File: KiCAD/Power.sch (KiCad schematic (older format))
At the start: 13 parts, among them J301 UJC-HP-3-SMT-TR, SW302 KXT 331 LHS

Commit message: Continue work on Schematics
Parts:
- removed BC301: BQ25157, XasPrints:DSBGA-20, symbol XasParts:BQ25157
- removed FID301: Fiducial, XasPrints:LiPo_150mAh, symbol Mechanical:Fiducial
- removed R301: 5k 0402, Resistor_SMD:R_0402_1005Metric, symbol Device:R_Small
- removed SW302: KXT 331 LHS, Button_Switch_SMD:SW_SPST_CK_KXT3, symbol Switch:SW_Push
- added CH301: BQ24232, Package_DFN_QFN:VQFN-16-1EP_3x3mm_P0.5mm_EP1.6x1.6mm_ThermalVias, symbol XasParts:BQ24232
- added R301, R302: 10k 0402, Resistor_SMD:R_0402_1005Metric, symbol Device:R
- added R? (x2): R_Small, symbol Device:R_Small
- added SW301: MIC94069, XasPrints:MLF-6-EP-P0.5mm, symbol XasParts:MIC94069
- C303: value 2.2uF 0402 -> 1uF 0603 16V; footprint Capacitor_SMD:C_0402_1005Metric -> Capacitor_SMD:C_0603_1608Metric
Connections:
- net labels added: +5V, MAIN_PWR_ON
- net labels removed: SCL, SDA
- wire segments 67 -> 83
- no-connect marks 5 -> 6
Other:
- moved on the sheet: BT301, C301, C302, C304, C305, D301, J301, PW301

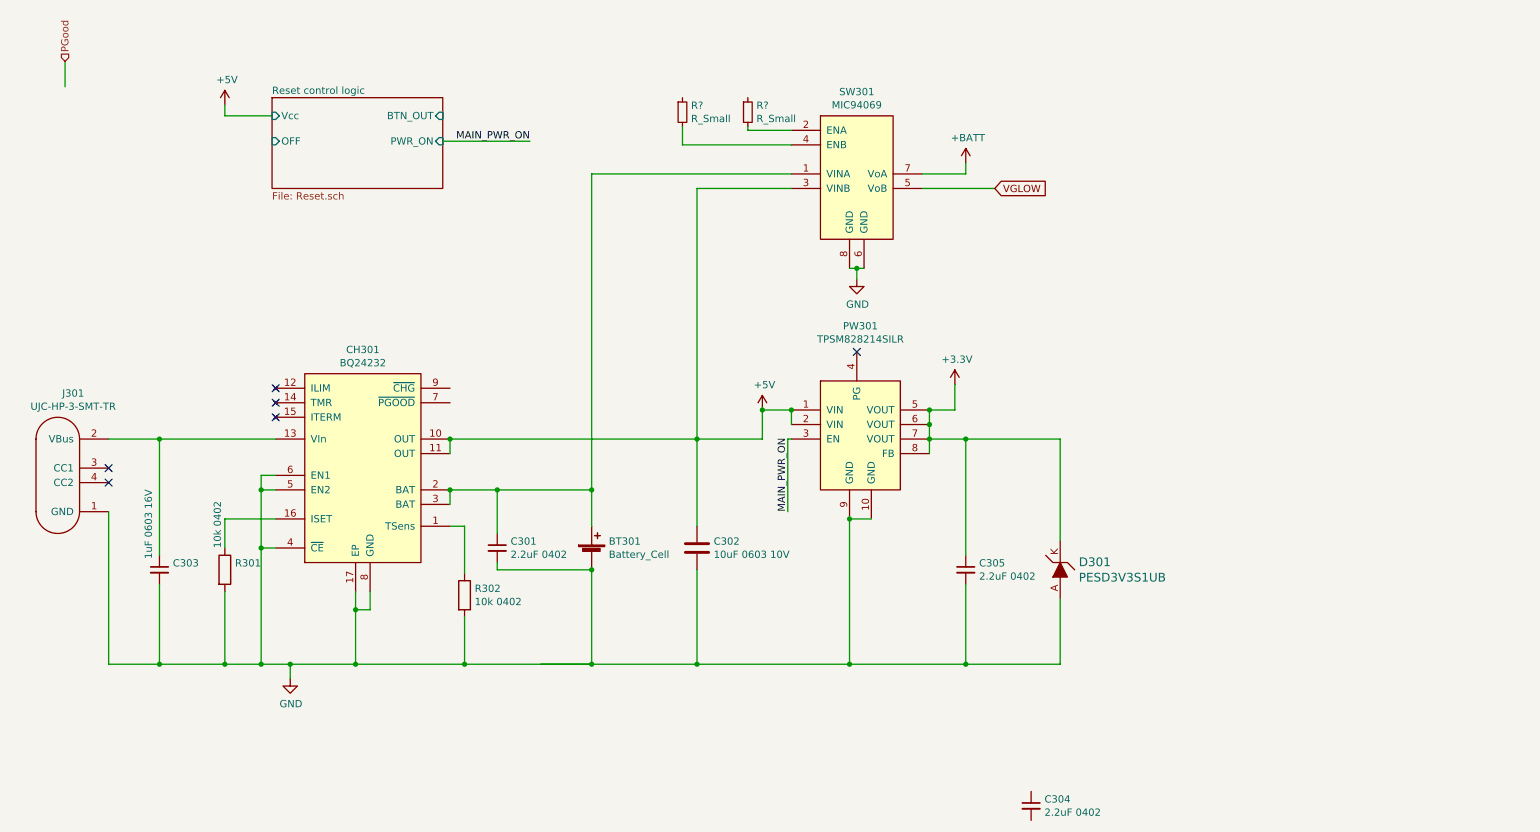
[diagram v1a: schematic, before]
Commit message: Add STM32 base circuit for power control and USB, also a lot of other things
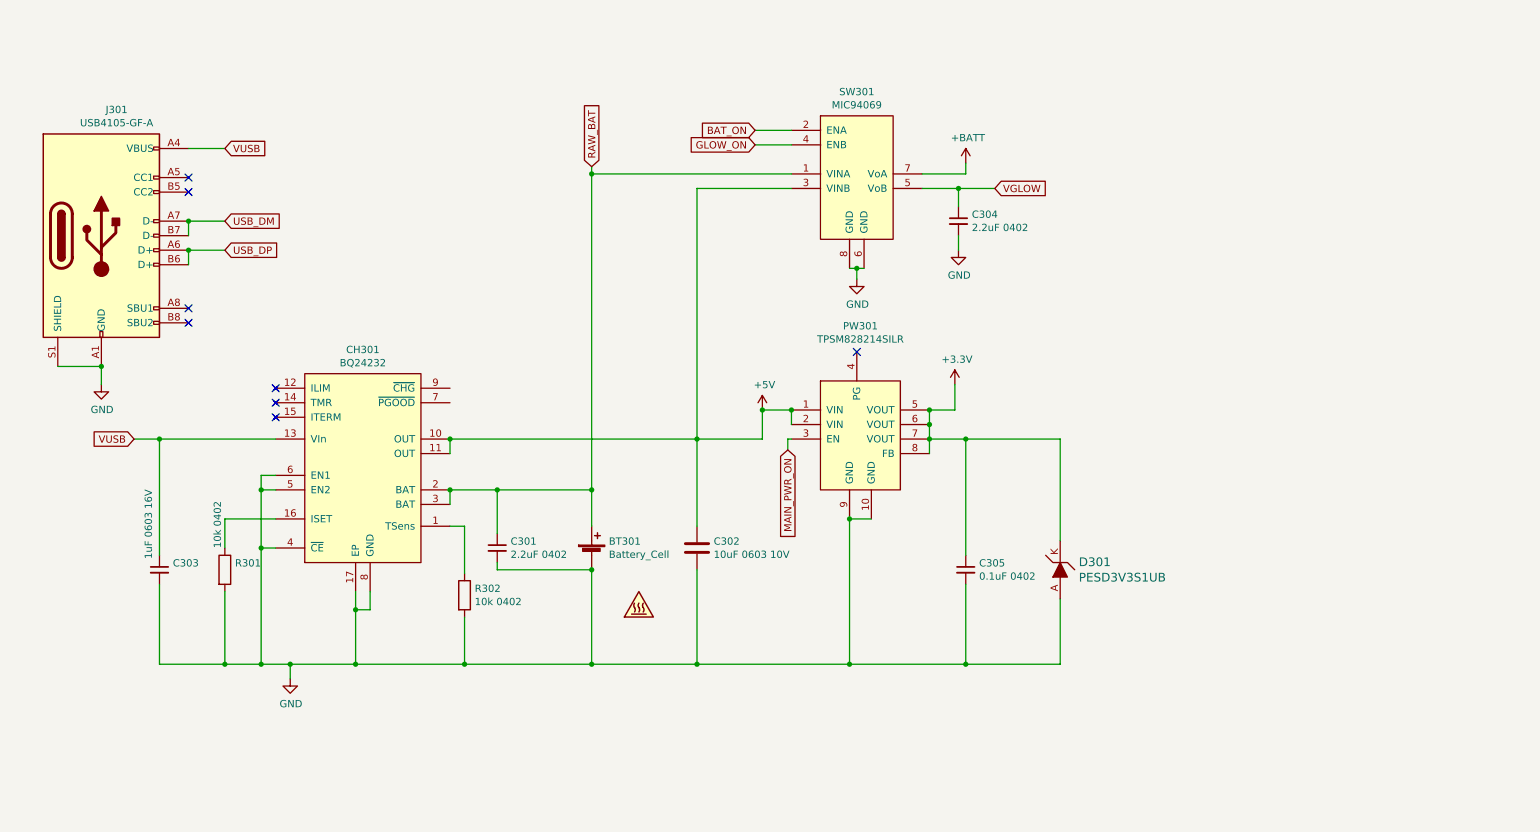
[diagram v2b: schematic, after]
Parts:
- removed J301: UJC-HP-3-SMT-TR, XasPrints:UJC-HP-3-SMT-TR, symbol XasParts:UJC-HP-3-SMT-TR
- removed R? (x2): R_Small, symbol Device:R_Small
- added BAT301: SYM_Hot_Small, XasPrints:LiPo_150mAh, symbol Graphic:SYM_Hot_Small
- added J301: USB4105-GF-A, Connector_USB:USB_C_Receptacle_HRO_TYPE-C-31-M-12, symbol Connector:USB_C_Receptacle_USB2.0
- C305: value 2.2uF 0402 -> 0.1uF 0402
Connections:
- net labels added: BAT_ON, GLOW_ON, RAW_BAT, USB_DM, USB_DP, VUSB
- net labels removed: PGood
- wire segments 83 -> 85
- no-connect marks 6 -> 8
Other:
- moved on the sheet: C304
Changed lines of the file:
@@
 $Descr A4 11693 8268
 encoding utf-8
-Sheet 3 7
+Sheet 3 6
 Title ""
 Date ""
@@
 L Device:C_Small C304
 U 1 1 60EEEDFC
-P 7575 6075
-F 0 "C304" H 7667 6121 50  0000 L CNN
-F 1 "2.2uF 0402" H 7667 6030 50  0000 L CNN
-F 2 "Capacitor_SMD:C_0402_1005Metric" H 7575 6075 50  0001 C CNN
-F 3 "~" H 7575 6075 50  0001 C CNN
-	1    7575 6075
+P 7075 2050
+F 0 "C304" H 7167 2096 50  0000 L CNN
+F 1 "2.2uF 0402" H 7167 2005 50  0000 L CNN
+F 2 "Capacitor_SMD:C_0402_1005Metric" H 7075 2050 50  0001 C CNN
+F 3 "~" H 7075 2050 50  0001 C CNN
+	1    7075 2050
 	1    0    0    -1
 $EndComp
@@
 P 7125 4450
 F 0 "C305" H 7217 4496 50  0000 L CNN
-F 1 "2.2uF 0402" H 7217 4405 50  0000 L CNN
+F 1 "0.1uF 0402" H 7217 4405 50  0000 L CNN
 F 2 "Capacitor_SMD:C_0402_1005Metric" H 7125 4450 50  0001 C CNN
 F 3 "~" H 7125 4450 50  0001 C CNN
@@
 $EndComp
 NoConn ~ 6375 2950
-Text HLabel 925  950  1    50   Input ~ 0
-PGood
-Wire Wire Line
-	925  950  925  1125
-$Comp
-L XasParts:UJC-HP-3-SMT-TR J301
-U 1 1 60F26A6F
-P 1125 4300
-F 0 "J301" H 981 5365 50  0000 C CNN
-F 1 "UJC-HP-3-SMT-TR" H 981 5274 50  0000 C CNN
-F 2 "XasPrints:UJC-HP-3-SMT-TR" H 1025 4200 50  0001 C CNN
-F 3 "https://www.cuidevices.com/product/resource/ujc-hp-3-smt-tr.pdf" H 1125 4300 50  0001 C CNN
-	1    1125 4300
-	1    0    0    -1
-$EndComp
-Wire Wire Line
-	1225 4050 1225 5100
-NoConn ~ 1225 3750
-NoConn ~ 1225 3850
 Wire Wire Line
 	3900 3900 4550 3900
@@
 Wire Wire Line
 	7775 3550 7775 4250
-$Sheet
-S 2350 1200 1175 625
-U 610325E4
-F0 "Reset control logic" 50
-F1 "Reset.sch" 50
-F2 "Vcc" I L 2350 1325 50
-F3 "BTN_OUT" I R 3525 1325 50
-F4 "OFF" I L 2350 1500 50
-F5 "PWR_ON" I R 3525 1500 50
-$EndSheet
 $Comp
 L XasParts:BQ24232 CH301
@@
 Connection ~ 3575 3550
 NoConn ~ 2375 3200
-Wire Wire Line
-	1225 3550 1575 3550
 $Comp
 L Device:C_Small C303
@@
 $EndComp
 Wire Wire Line
-	1225 5100 1575 5100
-Wire Wire Line
 	1575 4550 1575 5100
-Connection ~ 1575 5100
 Wire Wire Line
 	1575 4350 1575 3550
-Connection ~ 1575 3550
 NoConn ~ 2375 3300
 NoConn ~ 2375 3400
@@
 	2025 4100 2375 4100
 Wire Wire Line
-	2025 1250 2025 1325
-Wire Wire Line
-	2025 1325 2350 1325
-Wire Wire Line
-	3525 1500 4125 1500
-Text Label 4125 1500 2    50   ~ 0
-MAIN_PWR_ON
-Text Label 5900 4050 1    50   ~ 0
-MAIN_PWR_ON
-Wire Wire Line
 	5275 4150 5275 3550
 Connection ~ 5275 3550
@@
 	5925 3550 5900 3550
 Wire Wire Line
-	5900 3550 5900 4050
+	5900 3550 5900 3625
 Connection ~ 7125 5100
 Wire Wire Line
@@
 Wire Wire Line
 	2475 5100 2925 5100
-Wire Wire Line
-	4200 5100 4550 5100
 Wire Wire Line
 	3675 5100 4550 5100
@@
 Connection ~ 4550 3900
 Wire Wire Line
-	6825 1825 7325 1825
+	6825 1825 7075 1825
 $Comp
 L power:+5V #PWR0142
@@
 Connection ~ 5725 3350
 $Comp
-L power:+5V #PWR0128
-U 1 1 6110BDC6
-P 2025 1250
-F 0 "#PWR0128" H 2025 1100 50  0001 C CNN
-F 1 "+5V" H 2040 1423 50  0000 C CNN
-F 2 "" H 2025 1250 50  0001 C CNN
-F 3 "" H 2025 1250 50  0001 C CNN
-	1    2025 1250
-	1    0    0    -1
-$EndComp
-$Comp
-L Device:R_Small R?
-U 1 1 6110DFEC
-P 5625 1300
-F 0 "R?" H 5684 1346 50  0000 L CNN
-F 1 "R_Small" H 5684 1255 50  0000 L CNN
-F 2 "" H 5625 1300 50  0001 C CNN
-F 3 "~" H 5625 1300 50  0001 C CNN
-	1    5625 1300
-	1    0    0    -1
-$EndComp
-$Comp
-L Device:R_Small R?
-U 1 1 6110E052
-P 5175 1300
-F 0 "R?" H 5234 1346 50  0000 L CNN
-F 1 "R_Small" H 5234 1255 50  0000 L CNN
-F 2 "" H 5175 1300 50  0001 C CNN
-F 3 "~" H 5175 1300 50  0001 C CNN
-	1    5175 1300
-	1    0    0    -1
-$EndComp
-Wire Wire Line
-	5925 1425 5625 1425
-Wire Wire Line
-	5625 1425 5625 1400
-Wire Wire Line
-	5925 1525 5175 1525
-Wire Wire Line
-	5175 1525 5175 1400
+L Graphic:SYM_Hot_Small BAT301
+U 1 1 610A5342
+P 4875 4700
+F 0 "BAT301" H 4875 4840 50  0001 C CNN
+F 1 "SYM_Hot_Small" H 4875 4575 50  0001 C CNN
+F 2 "XasPrints:LiPo_150mAh" H 4875 4525 50  0001 C CNN
+F 3 "~" H 4905 4500 50  0001 C CNN
+	1    4875 4700
+	1    0    0    -1
+$EndComp
+Wire Wire Line
+	7075 1950 7075 1825
+Connection ~ 7075 1825
+Wire Wire Line
+	7075 1825 7325 1825
+$Comp
+L power:GND #PWR0149
+U 1 1 61125641
+P 7075 2250
+F 0 "#PWR0149" H 7075 2000 50  0001 C CNN
+F 1 "GND" H 7080 2077 50  0000 C CNN
+F 2 "" H 7075 2250 50  0001 C CNN
+F 3 "" H 7075 2250 50  0001 C CNN
+	1    7075 2250
+	1    0    0    -1
+$EndComp
+Wire Wire Line
+	7075 2250 7075 2150
+Text GLabel 4550 1675 1    50   Input ~ 0
+RAW_BAT
+Wire Wire Line
+	4550 1675 4550 1725
+Connection ~ 4550 1725
+$Comp
+L Connector:USB_C_Receptacle_USB2.0 J301
+U 1 1 611F4AA2
+P 1175 2150
+F 0 "J301" H 1280 3017 50  0000 C CNN
+F 1 "USB4105-GF-A" H 1280 2926 50  0000 C CNN
+F 2 "Connector_USB:USB_C_Receptacle_HRO_TYPE-C-31-M-12" H 1325 2150 50  0001 C CNN
+F 3 "https://www.usb.org/sites/default/files/documents/usb_type-c.zip" H 1325 2150 50  0001 C CNN
+	1    1175 2150
+	1    0    0    -1
+$EndComp
+Wire Wire Line
+	5925 1425 5675 1425
+Text GLabel 5675 1425 0    50   Input ~ 0
+BAT_ON
+Text GLabel 5675 1525 0    50   Input ~ 0
+GLOW_ON
+Wire Wire Line
+	5675 1525 5925 1525
+Text GLabel 2025 2050 2    50   Input ~ 0
+USB_DM
+Wire Wire Line
+	2025 2050 1775 2050
+Wire Wire Line
+	1775 2050 1775 2150
+Connection ~ 1775 2050
+Text GLabel 2025 2250 2    50   Input ~ 0
+USB_DP
+Wire Wire Line
+	2025 2250 1775 2250
+Wire Wire Line
+	1775 2250 1775 2350
+Connection ~ 1775 2250
+Wire Wire Line
+	875  3050 1175 3050
+$Comp
+L power:GND #PWR0153
+U 1 1 61283021
+P 1175 3175
+F 0 "#PWR0153" H 1175 2925 50  0001 C CNN
+F 1 "GND" H 1180 3002 50  0000 C CNN
+F 2 "" H 1175 3175 50  0001 C CNN
+F 3 "" H 1175 3175 50  0001 C CNN
+	1    1175 3175
+	1    0    0    -1
+$EndComp
+Wire Wire Line
+	1175 3175 1175 3050
+Connection ~ 1175 3050
+NoConn ~ 1775 2650
+NoConn ~ 1775 2750
+NoConn ~ 1775 1850
+NoConn ~ 1775 1750
+Text GLabel 2025 1550 2    50   Input ~ 0
+VUSB
+Wire Wire Line
+	2025 1550 1775 1550
+Text GLabel 1400 3550 0    50   Input ~ 0
+VUSB
+Wire Wire Line
+	1400 3550 1575 3550
+Connection ~ 1575 3550
+Text GLabel 5900 3625 3    50   Input ~ 0
+MAIN_PWR_ON
 $EndSCHEMATC

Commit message: Continue work on TapV2's schematic, almost completing it!
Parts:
- C303: value 1uF 0603 16V -> 1uF 0402 16V; footprint Capacitor_SMD:C_0603_1608Metric -> Capacitor_SMD:C_0402_1005Metric
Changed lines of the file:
@@
 AR Path="/61017570/6106B1C4" Ref="C?"  Part="1"
 F 0 "C303" H 1667 4496 50  0000 L CNN
-F 1 "1uF 0603 16V" V 1500 4525 50  0000 L CNN
-F 2 "Capacitor_SMD:C_0603_1608Metric" H 1575 4450 50  0001 C CNN
+F 1 "1uF 0402 16V" V 1500 4525 50  0000 L CNN
+F 2 "Capacitor_SMD:C_0402_1005Metric" H 1575 4450 50  0001 C CNN
 F 3 "~" H 1575 4450 50  0001 C CNN
 	1    1575 4450

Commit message: Finalize PCB schematics
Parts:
- added JP302, JP303: SolderJumper_3_Bridged12, Jumper:SolderJumper-3_P1.3mm_Open_RoundedPad1.0x1.5mm, symbol Jumper:SolderJumper_3_Bridged12
- added TP301: TestPoint, Connector_PinHeader_1.27mm:PinHeader_1x01_P1.27mm_Vertical, symbol Connector:TestPoint
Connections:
- net +3V3: now also JP303.3 (B)
- net +5V: now also JP302.1 (A)
- net BAT_ON: now also JP303.1 (A); no longer SW301.2 (ENA)
- net MAIN_PWR_ON: now also JP302.3 (B); no longer PW301.3 (EN)
- net VUSB: now also TP301.1
- net ~VUSB_PRESENT: now reaches CH301.7 (~PGOOD)
- net ~CHG: now reaches CH301.9 (~CHG)
- new net: JP302.2 (C), PW301.3 (EN)
- new net: JP303.2 (C), SW301.2 (ENA)
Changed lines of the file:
@@
 Wire Wire Line
 	5925 3550 5900 3550
-Wire Wire Line
-	5900 3550 5900 3625
 Connection ~ 7125 5100
 Wire Wire Line
@@
 	5275 1825 5275 3550
 Wire Wire Line
-	5925 1725 4550 1725
-Wire Wire Line
 	4550 1725 4550 3900
 Connection ~ 4550 3900
@@
 $EndComp
 Wire Wire Line
-	6825 1725 7125 1725
-Wire Wire Line
 	7125 1725 7125 1650
 Connection ~ 5725 3350
@@
 	1    0    0    -1
 $EndComp
-Wire Wire Line
-	5925 1425 5675 1425
-Text GLabel 5675 1425 0    50   Input ~ 0
+Text GLabel 4775 1050 0    50   Input ~ 0
 BAT_ON
 Text GLabel 5675 1525 0    50   Input ~ 0
@@
 	1400 3550 1575 3550
 Connection ~ 1575 3550
-Text GLabel 5900 3625 3    50   Input ~ 0
+Text GLabel 5575 5600 0    50   Input ~ 0
 MAIN_PWR_ON
+$Comp
+L Jumper:SolderJumper_3_Bridged12 JP302
+U 1 1 613FBF68
+P 5900 5600
+F 0 "JP302" H 5900 5712 50  0000 C CNN
+F 1 "SolderJumper_3_Bridged12" H 5900 5803 50  0000 C CNN
+F 2 "Jumper:SolderJumper-3_P1.3mm_Open_RoundedPad1.0x1.5mm" H 5900 5600 50  0001 C CNN
+F 3 "~" H 5900 5600 50  0001 C CNN
+	1    5900 5600
+	-1   0    0    1
+$EndComp
+Wire Wire Line
+	5575 5600 5700 5600
+Wire Wire Line
+	5900 3550 5900 5450
+$Comp
+L power:+5V #PWR0158
+U 1 1 61401BC7
+P 6150 5600
+F 0 "#PWR0158" H 6150 5450 50  0001 C CNN
+F 1 "+5V" H 6165 5773 50  0000 C CNN
+F 2 "" H 6150 5600 50  0001 C CNN
+F 3 "" H 6150 5600 50  0001 C CNN
+	1    6150 5600
+	0    1    1    0
+$EndComp
+Wire Wire Line
+	6150 5600 6100 5600
+$Comp
+L Connector:TestPoint TP301
+U 1 1 6147631B
+P 1575 3475
+F 0 "TP301" H 1633 3595 50  0000 L CNN
+F 1 "TestPoint" H 1633 3504 50  0000 L CNN
+F 2 "Connector_PinHeader_1.27mm:PinHeader_1x01_P1.27mm_Vertical" H 1775 3475 50  0001 C CNN
+F 3 "~" H 1775 3475 50  0001 C CNN
+	1    1575 3475
+	1    0    0    -1
+$EndComp
+Wire Wire Line
+	1575 3475 1575 3550
+Text GLabel 3750 3300 2    50   Input ~ 0
+~VUSB_PRESENT
+Text GLabel 3750 3175 2    50   Input ~ 0
+~CHG
+Wire Wire Line
+	3750 3175 3675 3175
+Wire Wire Line
+	3675 3175 3675 3200
+Wire Wire Line
+	3675 3200 3575 3200
+Wire Wire Line
+	3750 3300 3575 3300
+Wire Wire Line
+	4550 1725 5925 1725
+Wire Wire Line
+	6825 1725 7125 1725
+$Comp
+L Jumper:SolderJumper_3_Bridged12 JP303
+U 1 1 61427A8C
+P 5100 1050
+F 0 "JP303" H 5100 1162 50  0000 C CNN
+F 1 "SolderJumper_3_Bridged12" H 5100 1253 50  0000 C CNN
+F 2 "Jumper:SolderJumper-3_P1.3mm_Open_RoundedPad1.0x1.5mm" H 5100 1050 50  0001 C CNN
+F 3 "~" H 5100 1050 50  0001 C CNN
+	1    5100 1050
+	1    0    0    -1
+$EndComp
+Wire Wire Line
+	4775 1050 4900 1050
+Wire Wire Line
+	5100 1200 5100 1425
+Wire Wire Line
+	5100 1425 5925 1425
+Wire Wire Line
+	5300 1050 5775 1050
+Wire Wire Line
+	5775 1050 5775 950
+$Comp
+L power:+3.3V #PWR0163
+U 1 1 6142FA47
+P 5775 950
+F 0 "#PWR0163" H 5775 800 50  0001 C CNN
+F 1 "+3.3V" H 5790 1123 50  0000 C CNN
+F 2 "" H 5775 950 50  0001 C CNN
+F 3 "" H 5775 950 50  0001 C CNN
+	1    5775 950
+	1    0    0    -1
+$EndComp
 $EndSCHEMATC
